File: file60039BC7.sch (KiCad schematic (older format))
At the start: 32 parts, among them J3 Conn_01x06, U2 ATmega32U4, X1 XRCGB16M000FXN00R0

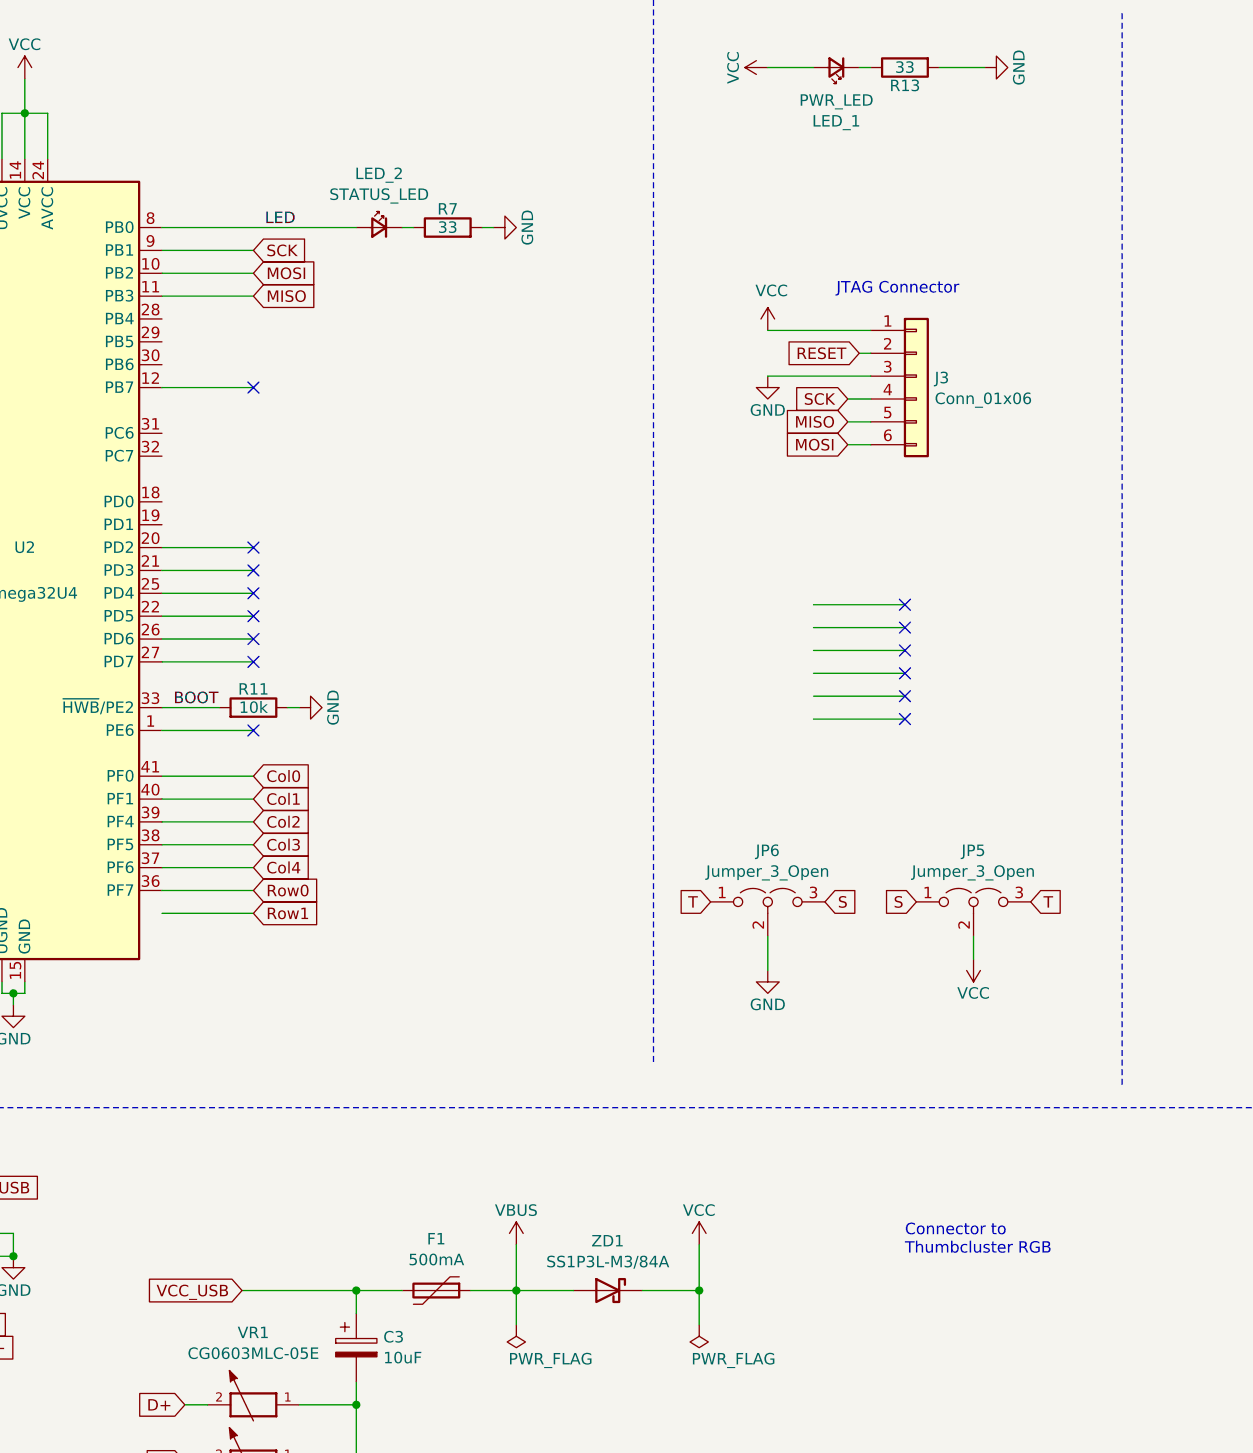
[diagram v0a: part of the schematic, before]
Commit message: plate added, step files
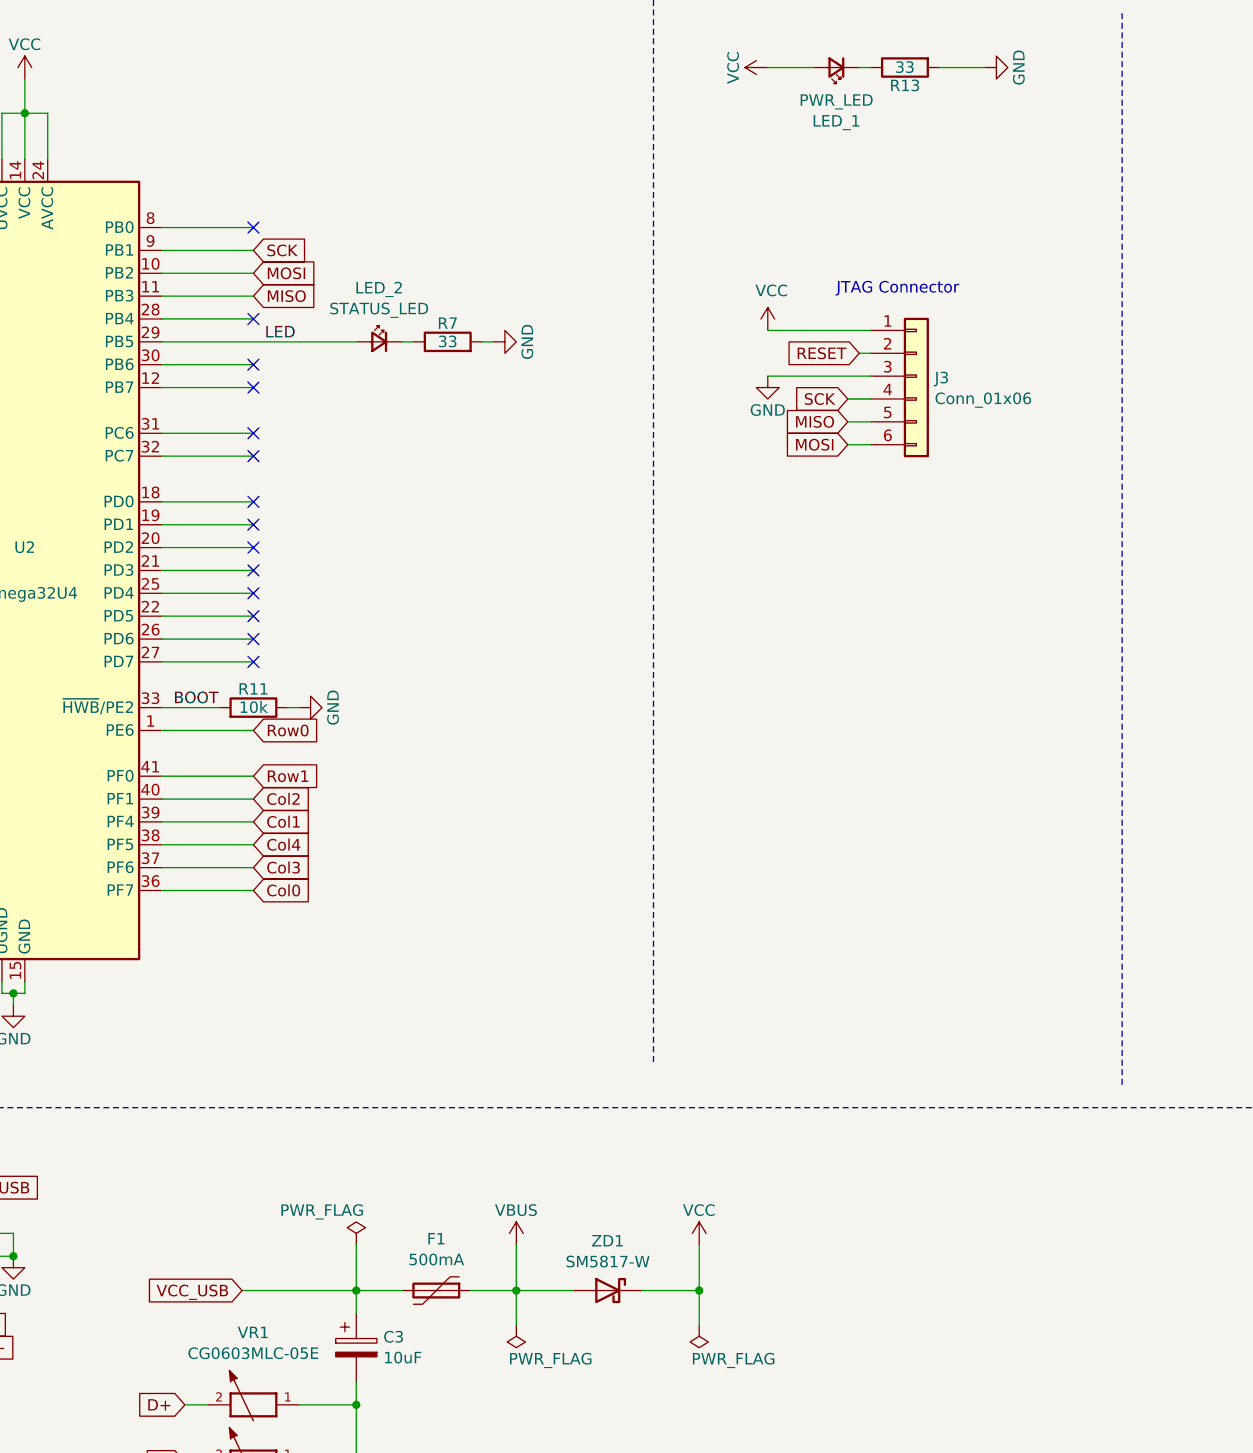
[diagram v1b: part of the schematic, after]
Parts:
- removed JP5, JP6: Jumper_3_Open, Keyboard 2:SolderJumper-3_P1.3mm_Bridged12_RoundedPad1.0x1.5mm_NumberLabels, symbol Jumper:Jumper_3_Open
- J3: footprint Keyboard 2:PinHeader_2x03_P1.27mm_Vertical -> Connector_PinHeader_2.54mm:PinHeader_2x03_P2.54mm_Vertical
- ZD1: value SS1P3L-M3/84A -> SM5817-W; footprint DIO_SS3P3-M3:84A -> Diode_SMD:D_MELF; Manufacturer_Part_Number SS1P3L-M3/84A -> SM5817-W
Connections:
- net labels removed: S, T
- wire segments 139 -> 138
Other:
- note removed: "Connector to \nThumbcluster RGB"
- moved on the sheet: LED_2, R7
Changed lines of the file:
@@
 Connection ~ 900  2050
 Wire Wire Line
-	6250 3400 6650 3400
+	3400 2750 3800 2750
 Wire Wire Line
 	3800 1850 3400 1850
@@
 UCAP
 Wire Wire Line
-	6250 3600 6650 3600
-Wire Wire Line
-	6250 3500 6650 3500
+	3400 1550 3800 1550
 Text GLabel 3800 1650 2    50   Input ~ 0
 SCK
@@
 	3400 3350 3800 3350
 Wire Wire Line
+	3400 4350 3800 4350
+Wire Wire Line
+	3400 3050 3800 3050
+Wire Wire Line
 	3400 4250 3800 4250
 Wire Wire Line
-	3400 3050 3800 3050
-Wire Wire Line
 	3400 4150 3800 4150
 Wire Wire Line
 	3400 4050 3800 4050
-Wire Wire Line
-	3400 3950 3800 3950
 $Comp
 L power:VBUS #PWR?
@@
 	1750 4000 2000 4000
 Wire Wire Line
-	6250 3200 6650 3200
-Wire Wire Line
-	6250 3300 6650 3300
+	3400 2450 3800 2450
+Wire Wire Line
+	3400 2550 3800 2550
 Wire Notes Line
 	750  5400 10800 5400
@@
 Wire Wire Line
 	1150 2650 1300 2650
-NoConn ~ 3800 3750
+NoConn ~ 3800 2850
 NoConn ~ 3800 2250
 Wire Wire Line
@@
 F 0 "J3" H 6780 2192 50  0000 L CNN
 F 1 "Conn_01x06" H 6780 2101 50  0000 L CNN
-F 2 "Keyboard 2:PinHeader_2x03_P1.27mm_Vertical" H 6700 2200 50  0001 C CNN
+F 2 "Connector_PinHeader_2.54mm:PinHeader_2x03_P2.54mm_Vertical" H 6700 2200 50  0001 C CNN
 F 3 "~" H 6700 2200 50  0001 C CNN
 F 4 "0" H 6700 2200 50  0001 C CNN "Fält4"
@@
 	1    0    0    -1
 $EndComp
-$Comp
-L power:VCC #PWR?
-U 1 1 5F7BBEF6
-P 6950 4750
-AR Path="/5D8219F0/5F7BBEF6" Ref="#PWR?"  Part="1"
-AR Path="/5D6CC2CC/5F7BBEF6" Ref="#PWR?"  Part="1"
-AR Path="/5DEF6A4C/5F7BBEF6" Ref="#PWR?"  Part="1"
-AR Path="/5D3D0542/5F7BBEF6" Ref="#PWR?"  Part="1"
-AR Path="/5E49A860/5F7BBEF6" Ref="#PWR?"  Part="1"
-AR Path="/5E135D8F/5F7BBEF6" Ref="#PWR0106"  Part="1"
-AR Path="/60039BC8/5F7BBEF6" Ref="#PWR0106"  Part="1"
-F 0 "#PWR0106" H 6950 4600 50  0001 C CNN
-F 1 "VCC" H 6950 4900 50  0000 C CNN
-F 2 "" H 6950 4750 50  0001 C CNN
-F 3 "" H 6950 4750 50  0001 C CNN
-	1    6950 4750
-	-1   0    0    1
-$EndComp
-$Comp
-L power:GND #PWR?
-U 1 1 5F7BC665
-P 6050 4800
-AR Path="/5D8219F0/5F7BC665" Ref="#PWR?"  Part="1"
-AR Path="/5D6CC2CC/5F7BC665" Ref="#PWR?"  Part="1"
-AR Path="/5E135D8F/5F7BC665" Ref="#PWR0107"  Part="1"
-AR Path="/60039BC8/5F7BC665" Ref="#PWR0107"  Part="1"
-F 0 "#PWR0107" H 6050 4550 50  0001 C CNN
-F 1 "GND" H 6050 4650 50  0000 C CNN
-F 2 "" H 6050 4800 50  0001 C CNN
-F 3 "" H 6050 4800 50  0001 C CNN
-	1    6050 4800
-	1    0    0    -1
-$EndComp
-Wire Wire Line
-	6650 3700 6250 3700
-Wire Wire Line
-	3400 4350 3800 4350
+Wire Wire Line
+	3400 4450 3800 4450
 NoConn ~ 3800 2950
 Wire Wire Line
 	2150 1300 2150 1550
-$Comp
-L Jumper:Jumper_3_Open JP5
-U 1 1 5F697B90
-P 6950 4500
-F 0 "JP5" H 6950 4724 50  0000 C CNN
-F 1 "Jumper_3_Open" H 6950 4633 50  0000 C CNN
-F 2 "Keyboard 2:SolderJumper-3_P1.3mm_Bridged12_RoundedPad1.0x1.5mm_NumberLabels" H 6950 4500 50  0001 C CNN
-F 3 "~" H 6950 4500 50  0001 C CNN
-F 4 "0" H 6950 4500 50  0001 C CNN "Fält4"
-F 5 "Jumper" H 6950 4500 50  0001 C CNN "Manufacturer_Part_Number"
-	1    6950 4500
-	1    0    0    -1
-$EndComp
-$Comp
-L Jumper:Jumper_3_Open JP6
-U 1 1 5F698B76
-P 6050 4500
-F 0 "JP6" H 6050 4724 50  0000 C CNN
-F 1 "Jumper_3_Open" H 6050 4633 50  0000 C CNN
-F 2 "Keyboard 2:SolderJumper-3_P1.3mm_Bridged12_RoundedPad1.0x1.5mm_NumberLabels" H 6050 4500 50  0001 C CNN
-F 3 "~" H 6050 4500 50  0001 C CNN
-F 4 "0" H 6050 4500 50  0001 C CNN "Fält4"
-F 5 "Jumper" H 6050 4500 50  0001 C CNN "Manufacturer_Part_Number"
-	1    6050 4500
-	1    0    0    -1
-$EndComp
-Wire Wire Line
-	6050 4800 6050 4650
-Wire Wire Line
-	6950 4650 6950 4750
-Text GLabel 5800 4500 0    50   Input ~ 0
-T
-Text GLabel 7200 4500 2    50   Input ~ 0
-T
-Text GLabel 6300 4500 2    50   Input ~ 0
-S
-Text GLabel 6700 4500 0    50   Input ~ 0
-S
 Wire Wire Line
 	3800 3150 3400 3150
 Wire Wire Line
-	3400 3750 3800 3750
+	3400 2850 3800 2850
 Wire Wire Line
 	3800 2250 3400 2250
@@
 AR Path="/60039BC8/5FB25345" Ref="ZD1"  Part="1"
 F 0 "ZD1" H 5350 6416 50  0000 C CNN
-F 1 "SS1P3L-M3/84A" H 5350 6325 50  0000 C CNN
-F 2 "DIO_SS3P3-M3:84A" H 5350 6200 50  0001 C CNN
+F 1 "SM5817-W" H 5350 6325 50  0000 C CNN
+F 2 "Diode_SMD:D_MELF" H 5350 6200 50  0001 C CNN
 F 3 "~" H 5350 6200 50  0001 C CNN
-F 4 "SS1P3L-M3/84A" H 5350 6200 50  0001 C CNN "Manufacturer_Part_Number"
+F 4 "SM5817-W" H 5350 6200 50  0001 C CNN "Manufacturer_Part_Number"
 F 5 "Vishay" H 5350 6200 50  0001 C CNN "Manufacturer_Name"
 F 6 "625-SS1P3L-M3/84A" H 5350 6200 50  0001 C CNN "Mouser Part Number"
@@
 Wire Wire Line
 	4450 6200 4250 6200
-Text Notes 6650 6050 0    50   ~ 0
-Connector to \nThumbcluster RGB
 Wire Wire Line
 	1250 2050 1450 2050
@@
 	1450 1600 2050 1600
 Wire Wire Line
-	4500 1550 4450 1550
+	4500 2050 4450 2050
 $Comp
 L Device:R R?
 U 1 1 5F8BDBBC
-P 4650 1550
+P 4650 2050
 AR Path="/5D8219F0/5F8BDBBC" Ref="R?"  Part="1"
 AR Path="/5D6CC2CC/5F8BDBBC" Ref="R?"  Part="1"
 AR Path="/5E135D8F/5F8BDBBC" Ref="R7"  Part="1"
 AR Path="/60039BC8/5F8BDBBC" Ref="R7"  Part="1"
-F 0 "R7" V 4730 1550 50  0000 C CNN
-F 1 "33" V 4650 1550 50  0000 C CNN
-F 2 "Resistor_SMD:R_0603_1608Metric" V 4580 1550 50  0001 C CNN
-F 3 "" H 4650 1550 50  0001 C CNN
-F 4 "1" H 4650 1550 50  0001 C CNN "Fält4"
-F 5 "Panasonic" H 4650 1550 50  0001 C CNN "Manufacturer_Name"
-F 6 "ERJ-3EKF33R0V" H 4650 1550 50  0001 C CNN "Manufacturer_Part_Number"
-F 7 "667-ERJ-3EKF33R0V" H 4650 1550 50  0001 C CNN "Mouser Part Number"
-	1    4650 1550
+F 0 "R7" V 4730 2050 50  0000 C CNN
+F 1 "33" V 4650 2050 50  0000 C CNN
+F 2 "Resistor_SMD:R_0603_1608Metric" V 4580 2050 50  0001 C CNN
+F 3 "" H 4650 2050 50  0001 C CNN
+F 4 "1" H 4650 2050 50  0001 C CNN "Fält4"
+F 5 "Panasonic" H 4650 2050 50  0001 C CNN "Manufacturer_Name"
+F 6 "ERJ-3EKF33R0V" H 4650 2050 50  0001 C CNN "Manufacturer_Part_Number"
+F 7 "667-ERJ-3EKF33R0V" H 4650 2050 50  0001 C CNN "Mouser Part Number"
+	1    4650 2050
 	0    -1   -1   0
 $EndComp
@@
 L Device:LED_Small LED_2
 U 1 1 5F8BDBC2
-P 4350 1550
-F 0 "LED_2" H 4350 1785 50  0000 C CNN
-F 1 "STATUS_LED" H 4350 1694 50  0000 C CNN
-F 2 "LED_SMD:LED_0603_1608Metric" V 4350 1550 50  0001 C CNN
-F 3 "~" V 4350 1550 50  0001 C CNN
-F 4 "1" H 4350 1550 50  0001 C CNN "Fält4"
-F 5 "Kingbright" H 4350 1550 50  0001 C CNN "Manufacturer_Name"
-F 6 "APT1608EC" H 4350 1550 50  0001 C CNN "Manufacturer_Part_Number"
-F 7 "604-APT1608EC" H 4350 1550 50  0001 C CNN "Mouser Part Number"
-	1    4350 1550
+P 4350 2050
+F 0 "LED_2" H 4350 2285 50  0000 C CNN
+F 1 "STATUS_LED" H 4350 2194 50  0000 C CNN
+F 2 "LED_SMD:LED_0603_1608Metric" V 4350 2050 50  0001 C CNN
+F 3 "~" V 4350 2050 50  0001 C CNN
+F 4 "1" H 4350 2050 50  0001 C CNN "Fält4"
+F 5 "Kingbright" H 4350 2050 50  0001 C CNN "Manufacturer_Name"
+F 6 "APT1608EC" H 4350 2050 50  0001 C CNN "Manufacturer_Part_Number"
+F 7 "604-APT1608EC" H 4350 2050 50  0001 C CNN "Mouser Part Number"
+	1    4350 2050
 	-1   0    0    -1
 $EndComp
 Wire Wire Line
-	4800 1550 4850 1550
+	4800 2050 4850 2050
 $Comp
 L power:GND #PWR?
 U 1 1 5F9F2D74
-P 4850 1550
+P 4850 2050
 AR Path="/5D8219F0/5F9F2D74" Ref="#PWR?"  Part="1"
 AR Path="/5D6CC2CC/5F9F2D74" Ref="#PWR?"  Part="1"
@@
 AR Path="/5E135D8F/5F9F2D74" Ref="#PWR0101"  Part="1"
 AR Path="/60039BC8/5F9F2D74" Ref="#PWR0101"  Part="1"
-F 0 "#PWR0101" H 4850 1300 50  0001 C CNN
-F 1 "GND" H 4850 1400 50  0000 C CNN
-F 2 "" H 4850 1550 50  0001 C CNN
-F 3 "" H 4850 1550 50  0001 C CNN
-	1    4850 1550
+F 0 "#PWR0101" H 4850 1800 50  0001 C CNN
+F 1 "GND" H 4850 1900 50  0000 C CNN
+F 2 "" H 4850 2050 50  0001 C CNN
+F 3 "" H 4850 2050 50  0001 C CNN
+	1    4850 2050
 	0    -1   1    0
 $EndComp
 Wire Wire Line
-	4250 1550 3400 1550
-Text Label 3850 1550 0    50   ~ 0
+	4250 2050 3400 2050
+Text Label 3850 2050 0    50   ~ 0
 LED
 $Comp
@@
 	3800 3250 3400 3250
 Wire Wire Line
-	3400 4550 3800 4550
-Wire Wire Line
-	3400 4450 3800 4450
+	3400 3950 3800 3950
+Wire Wire Line
+	3400 3750 3800 3750
 Wire Wire Line
 	1450 1300 2150 1300
 Wire Wire Line
 	900  1300 900  1600
+Text GLabel 3800 4450 2    50   Input ~ 0
+Col0
+Text GLabel 3800 4150 2    50   Input ~ 0
+Col1
+Text GLabel 3800 4050 2    50   Input ~ 0
+Col2
+Text GLabel 3800 4350 2    50   Input ~ 0
+Col3
+Text GLabel 3800 4250 2    50   Input ~ 0
+Col4
+Text GLabel 3800 3750 2    50   Input ~ 0
+Row0
 Text GLabel 3800 3950 2    50   Input ~ 0
-Col0
-Text GLabel 3800 4050 2    50   Input ~ 0
-Col1
-Text GLabel 3800 4150 2    50   Input ~ 0
-Col2
-Text GLabel 3800 4250 2    50   Input ~ 0
-Col3
-Text GLabel 3800 4350 2    50   Input ~ 0
-Col4
-Text GLabel 3800 4450 2    50   Input ~ 0
-Row0
-Text GLabel 3800 4550 2    50   Input ~ 0
 Row1
 NoConn ~ 3800 3150
 NoConn ~ 3800 3350
 NoConn ~ 3800 3450
-NoConn ~ 6650 3200
-NoConn ~ 6650 3300
-NoConn ~ 6650 3400
-NoConn ~ 6650 3500
-NoConn ~ 6650 3600
-NoConn ~ 6650 3700
+NoConn ~ 3800 2450
+NoConn ~ 3800 2550
+NoConn ~ 3800 2750
+NoConn ~ 3800 1550
+NoConn ~ 3800 2150
+Wire Wire Line
+	3800 2150 3400 2150
+NoConn ~ 3800 1950
+Wire Wire Line
+	3800 1950 3400 1950
+$Comp
+L power:PWR_FLAG #FLG?
+U 1 1 602567E1
+P 4250 6000
+AR Path="/5D8219F0/602567E1" Ref="#FLG?"  Part="1"
+AR Path="/5D6CC2CC/602567E1" Ref="#FLG?"  Part="1"
+AR Path="/5DEF6A4C/602567E1" Ref="#FLG?"  Part="1"
+AR Path="/5E49A860/602567E1" Ref="#FLG?"  Part="1"
+AR Path="/5E135D8F/602567E1" Ref="#FLG?"  Part="1"
+AR Path="/5F6ACAA0/602567E1" Ref="#FLG?"  Part="1"
+AR Path="/5F577A4E/602567E1" Ref="#FLG?"  Part="1"
+AR Path="/60039BC8/602567E1" Ref="#FLG0101"  Part="1"
+F 0 "#FLG0101" H 4250 6075 50  0001 C CNN
+F 1 "PWR_FLAG" H 4100 6150 50  0000 C CNN
+F 2 "" H 4250 6000 50  0001 C CNN
+F 3 "" H 4250 6000 50  0001 C CNN
+	1    4250 6000
+	1    0    0    -1
+$EndComp
+Wire Wire Line
+	4250 6000 4250 6200
 $EndSCHEMATC
